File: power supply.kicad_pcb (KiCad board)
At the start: 2 copper layers, 97.8 x 82.5 mm, 43 parts, among them J1 CONN_01X02_FEMALE, J2 CONN_01X02_FEMALE, Q1 PN2222A, U1 LT3080, U2 LM324

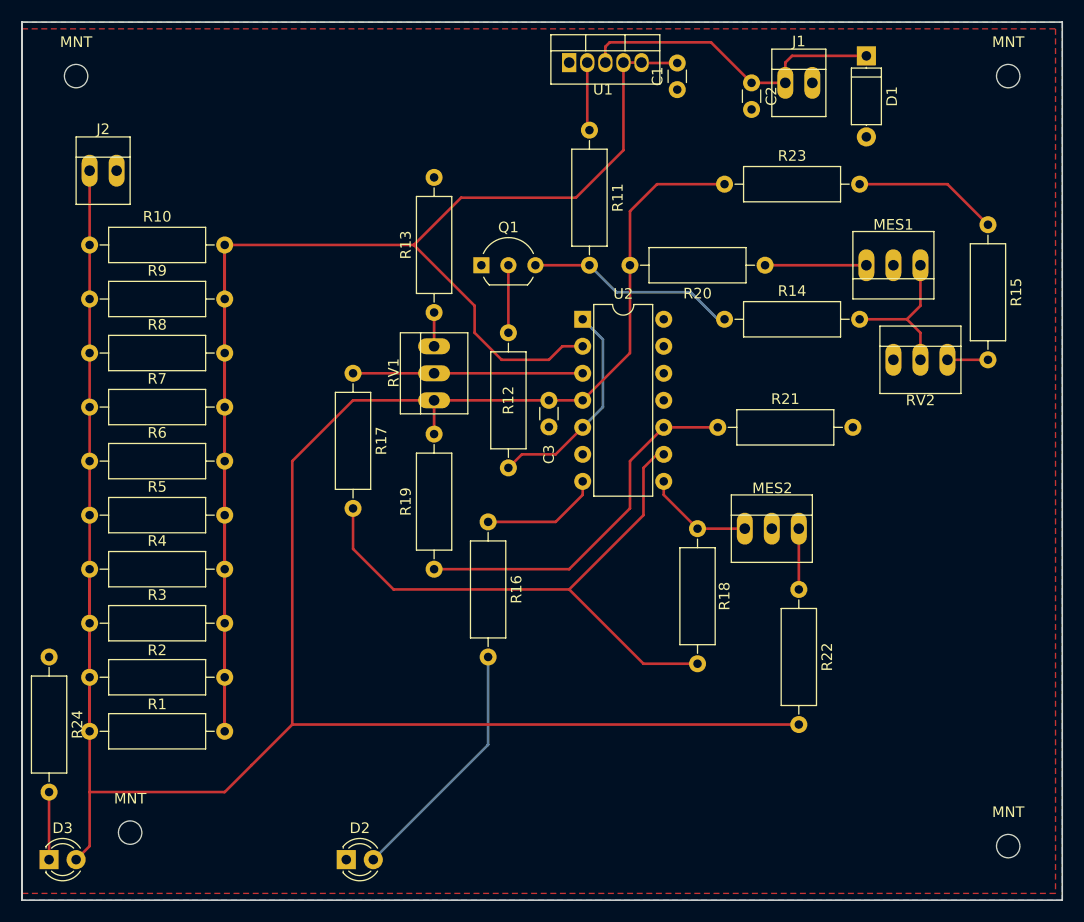
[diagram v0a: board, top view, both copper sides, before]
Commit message: Thicker traces for high-power rails
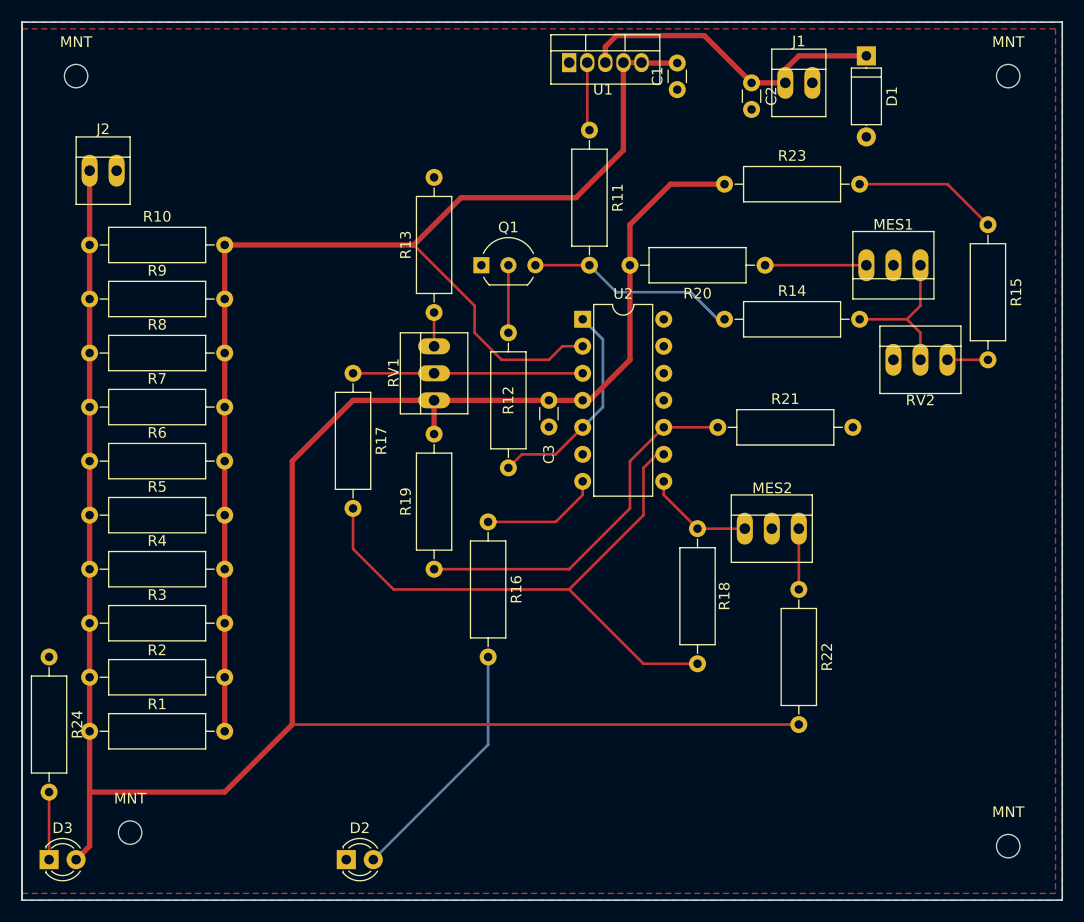
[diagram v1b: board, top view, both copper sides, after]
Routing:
- net +12V: track 248.4 -> 359.0 mm
- net /Isense: track 173.4 -> 273.6 mm
- net /OUT: track 30.0 -> 33.3 mm
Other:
- net class Power added: clearance 0.4, trace_width 0.5, via_dia 0.6, via_drill 0.4
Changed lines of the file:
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@@
     (thickness 1.6)
     (drawings 5)
-    (tracks 112)
+    (tracks 148)
     (zones 0)
     (modules 43)
@@
   (layers
     (0 F.Cu signal)
-    (31 B.Cu signal)
+    (31 B.Cu signal hide)
     (32 B.Adhes user)
     (33 F.Adhes user)
@@
     (uvia_dia 0.3)
     (uvia_drill 0.1)
-    (add_net +12V)
-    (add_net /Isense)
     (add_net /Iset)
-    (add_net /OUT)
     (add_net /Vset)
     (add_net GND)
@@
     (add_net "Net-(R17-Pad2)")
     (add_net "Net-(R19-Pad1)")
+  )
+  (net_class Power ""
+    (clearance 0.4)
+    (trace_width 0.5)
+    (via_dia 0.6)
+    (via_drill 0.4)
+    (uvia_dia 0.3)
+    (uvia_drill 0.1)
+    (add_net +12V)
+    (add_net /Isense)
+    (add_net /OUT)
   )
   (module Capacitors_THT:C_Disc_D3.0mm_W1.6mm_P2.50mm (layer F.Cu)
@@
   (gr_line (start 20.32 99.06) (end 20.32 16.51) (angle 90) (layer Edge.Cuts) (width 0.15))
   (gr_line (start 20.32 99.06) (end 20.32 16.51) (angle 90) (layer Edge.Cuts) (width 0.15))
-  (segment (start 77.47 39.37) (end 77.47 34.29) (width 0.25) (layer F.Cu) (net 2))
-  (segment (start 80.01 31.75) (end 86.36 31.75) (width 0.25) (layer F.Cu) (net 2))
-  (segment (start 77.47 34.29) (end 80.01 31.75) (width 0.25) (layer F.Cu) (net 2))
-  (segment (start 26.67 88.9) (end 39.37 88.9) (width 0.25) (layer F.Cu) (net 2))
+  (segment (start 77.47 39.37) (end 77.47 35.56) (width 0.5) (layer F.Cu) (net 2) (status 400000))
+  (segment (start 77.47 35.56) (end 81.28 31.75) (width 0.5) (layer F.Cu) (net 2))
+  (segment (start 81.28 31.75) (end 86.36 31.75) (width 0.5) (layer F.Cu) (net 2) (status 800000))
+  (segment (start 73.025 52.07) (end 73.66 52.07) (width 0.5) (layer F.Cu) (net 2) (status C00000))
+  (segment (start 73.66 52.07) (end 77.47 48.26) (width 0.5) (layer F.Cu) (net 2) (status 400000))
+  (segment (start 77.47 48.26) (end 77.47 39.37) (width 0.5) (layer F.Cu) (net 2) (status 800000))
+  (segment (start 59.055 52.07) (end 59.055 55.245) (width 0.5) (layer F.Cu) (net 2))
+  (segment (start 59.055 52.07) (end 69.85 52.07) (width 0.5) (layer F.Cu) (net 2))
+  (segment (start 69.85 52.07) (end 73.025 52.07) (width 0.5) (layer F.Cu) (net 2))
+  (segment (start 26.67 88.9) (end 39.37 88.9) (width 0.5) (layer F.Cu) (net 2))
+  (segment (start 39.37 88.9) (end 45.72 82.55) (width 0.5) (layer F.Cu) (net 2))
+  (segment (start 45.72 82.55) (end 45.72 57.785) (width 0.5) (layer F.Cu) (net 2))
+  (segment (start 45.72 57.785) (end 51.435 52.07) (width 0.5) (layer F.Cu) (net 2))
+  (segment (start 51.435 52.07) (end 59.055 52.07) (width 0.5) (layer F.Cu) (net 2))
+  (segment (start 26.67 30.48) (end 26.67 37.465) (width 0.5) (layer F.Cu) (net 2))
+  (segment (start 26.67 37.465) (end 26.67 42.545) (width 0.5) (layer F.Cu) (net 2))
+  (segment (start 26.67 42.545) (end 26.67 47.625) (width 0.5) (layer F.Cu) (net 2))
+  (segment (start 26.67 47.625) (end 26.67 52.705) (width 0.5) (layer F.Cu) (net 2))
+  (segment (start 26.67 52.705) (end 26.67 57.785) (width 0.5) (layer F.Cu) (net 2))
+  (segment (start 26.67 57.785) (end 26.67 62.865) (width 0.5) (layer F.Cu) (net 2))
+  (segment (start 26.67 62.865) (end 26.67 67.945) (width 0.5) (layer F.Cu) (net 2))
+  (segment (start 26.67 67.945) (end 26.67 73.025) (width 0.5) (layer F.Cu) (net 2))
+  (segment (start 26.67 73.025) (end 26.67 78.105) (width 0.5) (layer F.Cu) (net 2))
+  (segment (start 26.67 78.105) (end 26.67 83.185) (width 0.5) (layer F.Cu) (net 2))
+  (segment (start 26.67 83.185) (end 26.67 93.98) (width 0.5) (layer F.Cu) (net 2))
+  (segment (start 26.67 93.98) (end 25.4 95.25) (width 0.5) (layer F.Cu) (net 2))
   (segment (start 39.37 88.9) (end 41.91 86.36) (width 0.25) (layer F.Cu) (net 2))
   (segment (start 26.67 83.185) (end 26.67 88.9) (width 0.25) (layer F.Cu) (net 2))
@@
   (segment (start 45.72 82.55) (end 93.345 82.55) (width 0.25) (layer F.Cu) (net 2))
   (segment (start 41.91 86.36) (end 45.72 82.55) (width 0.25) (layer F.Cu) (net 2))
-  (segment (start 77.47 39.37) (end 77.47 47.625) (width 0.25) (layer F.Cu) (net 2))
-  (segment (start 77.47 47.625) (end 73.025 52.07) (width 0.25) (layer F.Cu) (net 2))
-  (segment (start 59.055 52.07) (end 59.055 55.245) (width 0.25) (layer F.Cu) (net 2))
-  (segment (start 59.055 52.07) (end 69.85 52.07) (width 0.25) (layer F.Cu) (net 2))
   (segment (start 73.025 52.07) (end 69.85 52.07) (width 0.25) (layer F.Cu) (net 2))
-  (segment (start 26.67 30.48) (end 26.67 37.465) (width 0.25) (layer F.Cu) (net 2))
   (segment (start 26.67 67.945) (end 26.67 73.025) (width 0.25) (layer F.Cu) (net 2))
   (segment (start 26.67 73.025) (end 26.67 78.105) (width 0.25) (layer F.Cu) (net 2))
@@
   (segment (start 70.485 63.5) (end 64.135 63.5) (width 0.25) (layer F.Cu) (net 12))
   (segment (start 73.025 60.96) (end 70.485 63.5) (width 0.25) (layer F.Cu) (net 12))
+  (segment (start 39.37 37.465) (end 57.15 37.465) (width 0.5) (layer F.Cu) (net 13) (status 400000))
+  (segment (start 57.15 37.465) (end 61.595 33.02) (width 0.5) (layer F.Cu) (net 13))
+  (segment (start 61.595 33.02) (end 72.39 33.02) (width 0.5) (layer F.Cu) (net 13))
+  (segment (start 72.39 33.02) (end 76.855 28.555) (width 0.5) (layer F.Cu) (net 13))
+  (segment (start 76.855 28.555) (end 76.855 22.02) (width 0.5) (layer F.Cu) (net 13))
+  (segment (start 76.855 22.02) (end 76.855 20.32) (width 0.5) (layer F.Cu) (net 13) (status 800000))
+  (segment (start 76.855 20.32) (end 78.555 20.32) (width 0.5) (layer F.Cu) (net 13) (status C00000))
+  (segment (start 78.555 20.32) (end 78.595 20.36) (width 0.5) (layer F.Cu) (net 13) (status C00000))
+  (segment (start 78.595 20.36) (end 81.915 20.36) (width 0.5) (layer F.Cu) (net 13) (status C00000))
+  (segment (start 39.37 37.465) (end 39.37 42.545) (width 0.5) (layer F.Cu) (net 13) (status C00000))
+  (segment (start 39.37 42.545) (end 39.37 47.625) (width 0.5) (layer F.Cu) (net 13) (status C00000))
+  (segment (start 39.37 47.625) (end 39.37 52.705) (width 0.5) (layer F.Cu) (net 13) (status C00000))
+  (segment (start 39.37 52.705) (end 39.37 57.785) (width 0.5) (layer F.Cu) (net 13) (status C00000))
+  (segment (start 39.37 57.785) (end 39.37 62.865) (width 0.5) (layer F.Cu) (net 13) (status C00000))
+  (segment (start 39.37 62.865) (end 39.37 67.945) (width 0.5) (layer F.Cu) (net 13) (status C00000))
+  (segment (start 39.37 67.945) (end 39.37 73.025) (width 0.5) (layer F.Cu) (net 13) (status C00000))
+  (segment (start 39.37 73.025) (end 39.37 78.105) (width 0.5) (layer F.Cu) (net 13) (status C00000))
+  (segment (start 39.37 78.105) (end 39.37 83.185) (width 0.5) (layer F.Cu) (net 13) (status C00000))
   (segment (start 57.15 37.465) (end 61.595 33.02) (width 0.25) (layer F.Cu) (net 13))
   (segment (start 76.855 28.555) (end 76.855 20.32) (width 0.25) (layer F.Cu) (net 13))
@@
   (segment (start 39.37 47.625) (end 39.37 42.545) (width 0.25) (layer F.Cu) (net 13))
   (segment (start 39.37 42.545) (end 39.37 37.465) (width 0.25) (layer F.Cu) (net 13))
-  (segment (start 99.695 19.685) (end 92.71 19.685) (width 0.25) (layer F.Cu) (net 14))
-  (segment (start 92.075 20.32) (end 92.075 22.225) (width 0.25) (layer F.Cu) (net 14))
-  (segment (start 92.71 19.685) (end 92.075 20.32) (width 0.25) (layer F.Cu) (net 14))
-  (segment (start 75.155 20.32) (end 75.155 18.825) (width 0.25) (layer F.Cu) (net 14))
-  (segment (start 85.09 18.415) (end 88.9 22.225) (width 0.25) (layer F.Cu) (net 14))
-  (segment (start 75.565 18.415) (end 85.09 18.415) (width 0.25) (layer F.Cu) (net 14))
-  (segment (start 75.155 18.825) (end 75.565 18.415) (width 0.25) (layer F.Cu) (net 14))
+  (segment (start 92.075 22.225) (end 92.075 20.955) (width 0.5) (layer F.Cu) (net 14))
+  (segment (start 92.075 20.955) (end 93.345 19.685) (width 0.5) (layer F.Cu) (net 14))
+  (segment (start 93.345 19.685) (end 99.695 19.685) (width 0.5) (layer F.Cu) (net 14))
+  (segment (start 75.155 20.32) (end 75.155 18.825) (width 0.5) (layer F.Cu) (net 14))
+  (segment (start 75.155 18.825) (end 76.2 17.78) (width 0.5) (layer F.Cu) (net 14))
+  (segment (start 84.455 17.78) (end 88.9 22.225) (width 0.5) (layer F.Cu) (net 14))
+  (segment (start 76.2 17.78) (end 84.455 17.78) (width 0.5) (layer F.Cu) (net 14))
+  (segment (start 88.9 22.225) (end 92.075 22.225) (width 0.5) (layer F.Cu) (net 14))
   (segment (start 88.9 22.225) (end 92.075 22.225) (width 0.25) (layer F.Cu) (net 14))
   (segment (start 103.505 44.45) (end 104.775 45.72) (width 0.25) (layer F.Cu) (net 15))

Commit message: Fix pin orientation on voltmeters
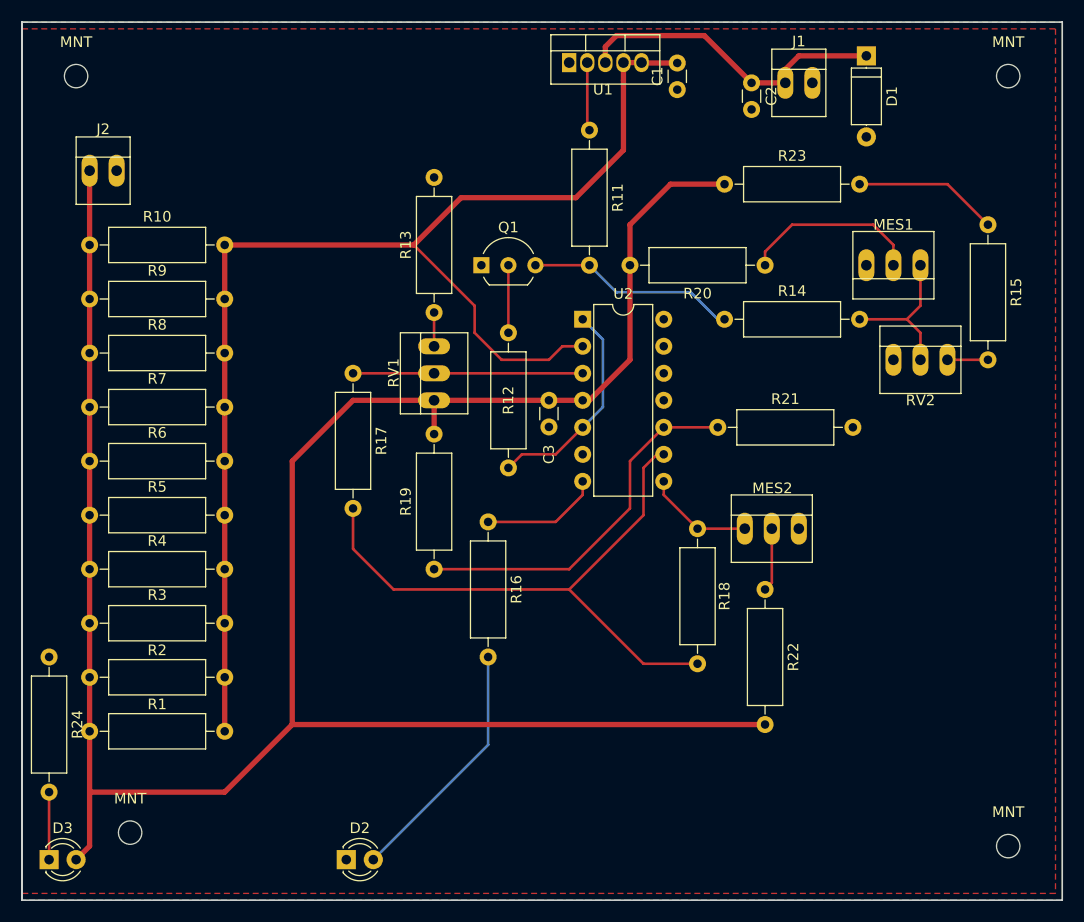
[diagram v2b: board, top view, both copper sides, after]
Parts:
- moved R22 3.17 mm to (90.2, 69.8)
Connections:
- MES1 pad 2: GND -> Net-(MES1-Pad2)
- MES1 pad 3: Net-(MES1-Pad3) -> GND
- MES2 pad 2: GND -> Net-(MES2-Pad2)
- MES2 pad 3: Net-(MES2-Pad3) -> GND
- R20 pad 1: Net-(MES1-Pad3) -> Net-(MES1-Pad2)
- R22 pad 1: Net-(MES2-Pad3) -> Net-(MES2-Pad2)
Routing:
- net Net-(MES1-Pad2): track 0.00 -> 17.1 mm
- net Net-(MES1-Pad3): track 9.52 -> 0.00 mm
- net Net-(MES2-Pad2): track 0.00 -> 5.98 mm
- net Net-(MES2-Pad3): track 5.71 -> 0.00 mm
- net +12V: track 359.0 -> 355.8 mm
